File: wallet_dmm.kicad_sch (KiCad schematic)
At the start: 0 parts

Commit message: Added piezo driver oscillator (based on TLC555CDR) to schematic. Needs component values calculated for oscillator parameters (frequency, etc).
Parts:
- added C1, C2: 0.01uF, symbol Device:C_Small
- added C3: C, symbol Device:C_Small
- added R1, R2: R, symbol Device:R
- added U1: TLC555xD, Package_SO:SOIC-8_3.9x4.9mm_P1.27mm, symbol Timer:TLC555xD
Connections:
- new net: R1.2, R2.1, U1.7 (DIS)
- new net: C1.1, U1.5 (CV)
- new net: C3.1, R2.2, U1.2 (TR), U1.6 (THR)
- new net GND: C1.2, C2.2, C3.2, U1.1 (GND)
- new net OSC_OUT: U1.3 (Q)
- new net VCC: C2.1, R1.1, U1.4 (R), U1.8 (VCC)
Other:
- note added: "Piezo Driver Oscillator"

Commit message: saving work
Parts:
- added U2: STM32L051K8Tx, Package_QFP:LQFP-32_7x7mm_P0.8mm, symbol MCU_ST_STM32L0:STM32L051K8Tx
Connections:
- net GND: now also U2.16 (VSS), U2.32 (VSS)
- new net VDD: U2.1 (VDD), U2.17 (VDD)
- new net VDDA: U2.5 (VDDA)

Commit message: test2
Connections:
- net GND: no longer U2.16 (VSS), U2.32 (VSS)
- net VDD: no longer U2.1 (VDD), U2.17 (VDD)
- net VDDA: no longer U2.5 (VDDA)
- new net: U2.16 (VSS), U2.32 (VSS)
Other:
- moved on the sheet: U2
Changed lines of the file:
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@@
 	(symbol
 		(lib_id "MCU_ST_STM32L0:STM32L051K8Tx")
-		(at 58.42 102.87 0)
+		(at 49.53 102.87 0)
 		(unit 1)
 		(exclude_from_sim no)
@@
 		(fields_autoplaced yes)
 		(property "Reference" "U2"
-			(at 63.1541 128.27 0)
+			(at 54.2641 128.27 0)
 			(effects
 				(font
@@
 		)
 		(property "Value" "STM32L051K8Tx"
-			(at 63.1541 130.81 0)
+			(at 54.2641 130.81 0)
 			(effects
 				(font
@@
 		)
 		(property "Footprint" "Package_QFP:LQFP-32_7x7mm_P0.8mm"
-			(at 48.26 125.73 0)
+			(at 39.37 125.73 0)
 			(effects
 				(font
@@
 		)
 		(property "Datasheet" "https://www.st.com/resource/en/datasheet/stm32l051k8.pdf"
-			(at 58.42 102.87 0)
+			(at 49.53 102.87 0)
 			(effects
 				(font
@@
 		)
 		(property "Description" "STMicroelectronics Arm Cortex-M0+ MCU, 64KB flash, 8KB RAM, 32 MHz, 1.65-3.6V, 25 GPIO, LQFP32"
-			(at 58.42 102.87 0)
+			(at 49.53 102.87 0)
 			(effects
 				(font

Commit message: UPDATE SKETCH FILE
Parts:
- C3: value C -> 100nF
- R1: value R -> 1510R
- R2: value R -> 1000R
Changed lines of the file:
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@@
 			)
 		)
-		(property "Value" "R"
+		(property "Value" "1000R"
 			(at 74.93 41.9099 0)
 			(effects
@@
 			)
 		)
-		(property "Value" "R"
+		(property "Value" "1510R"
 			(at 74.93 29.2099 0)
 			(effects
@@
 			)
 		)
-		(property "Value" "C"
+		(property "Value" "100nF"
 			(at 74.93 52.0762 0)
 			(effects

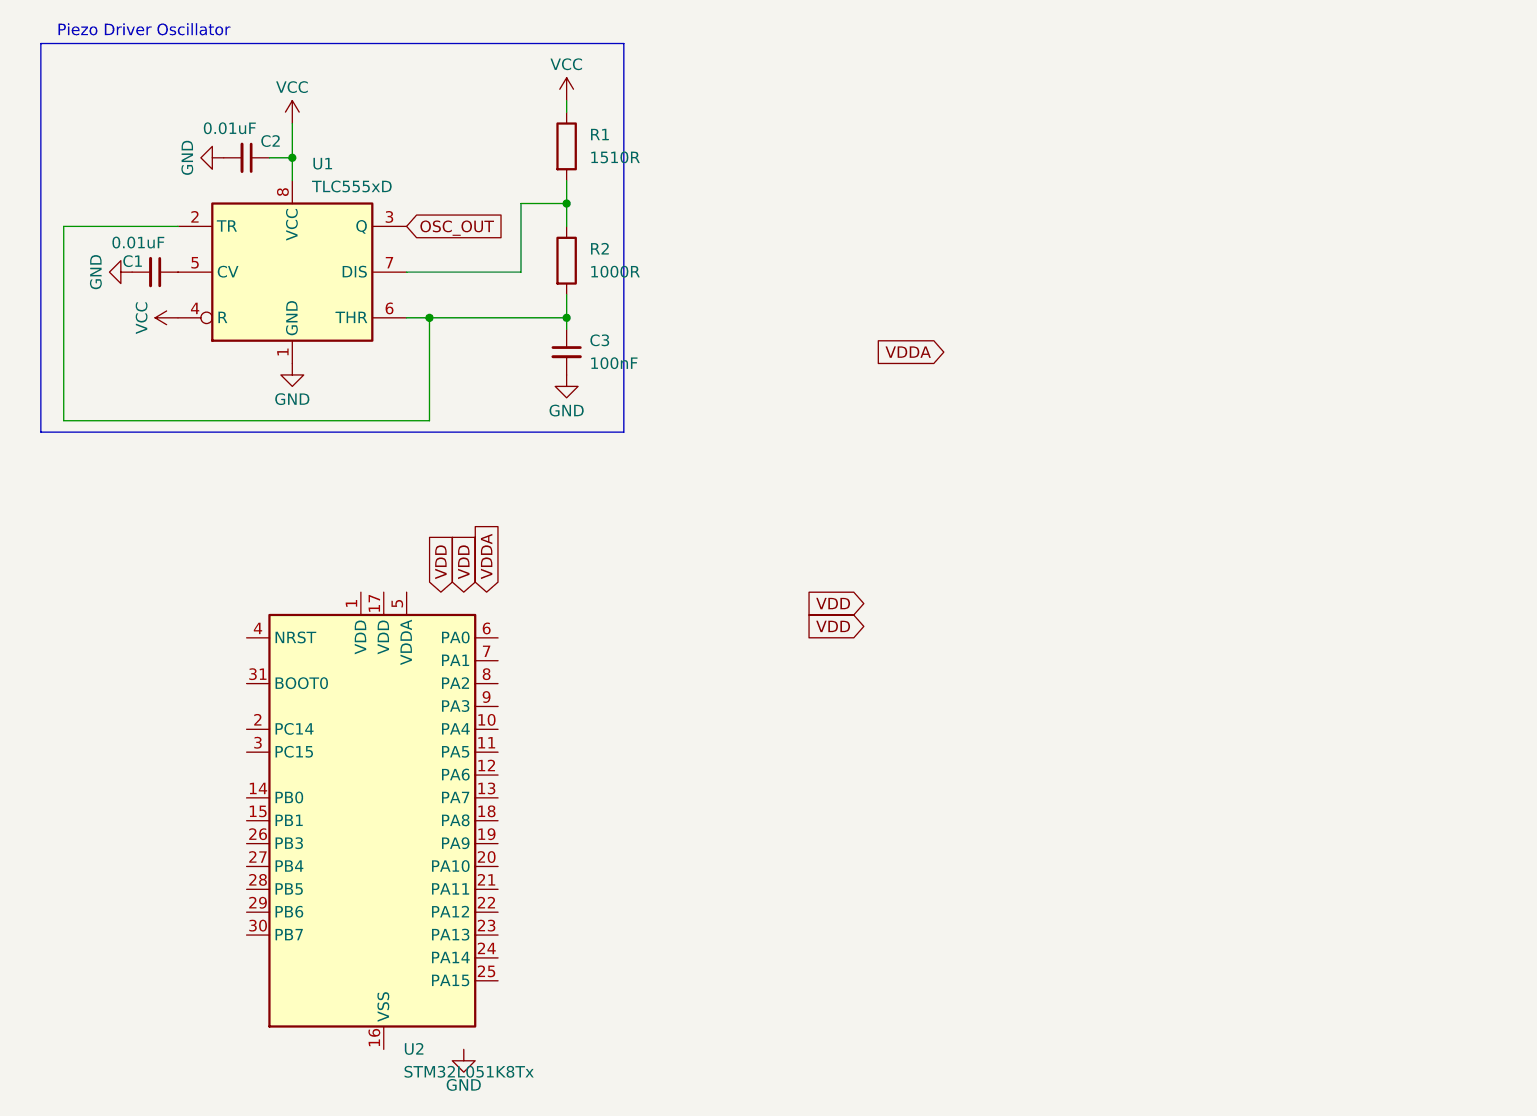
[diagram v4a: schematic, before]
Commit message: Added filter capacitors and reset button.
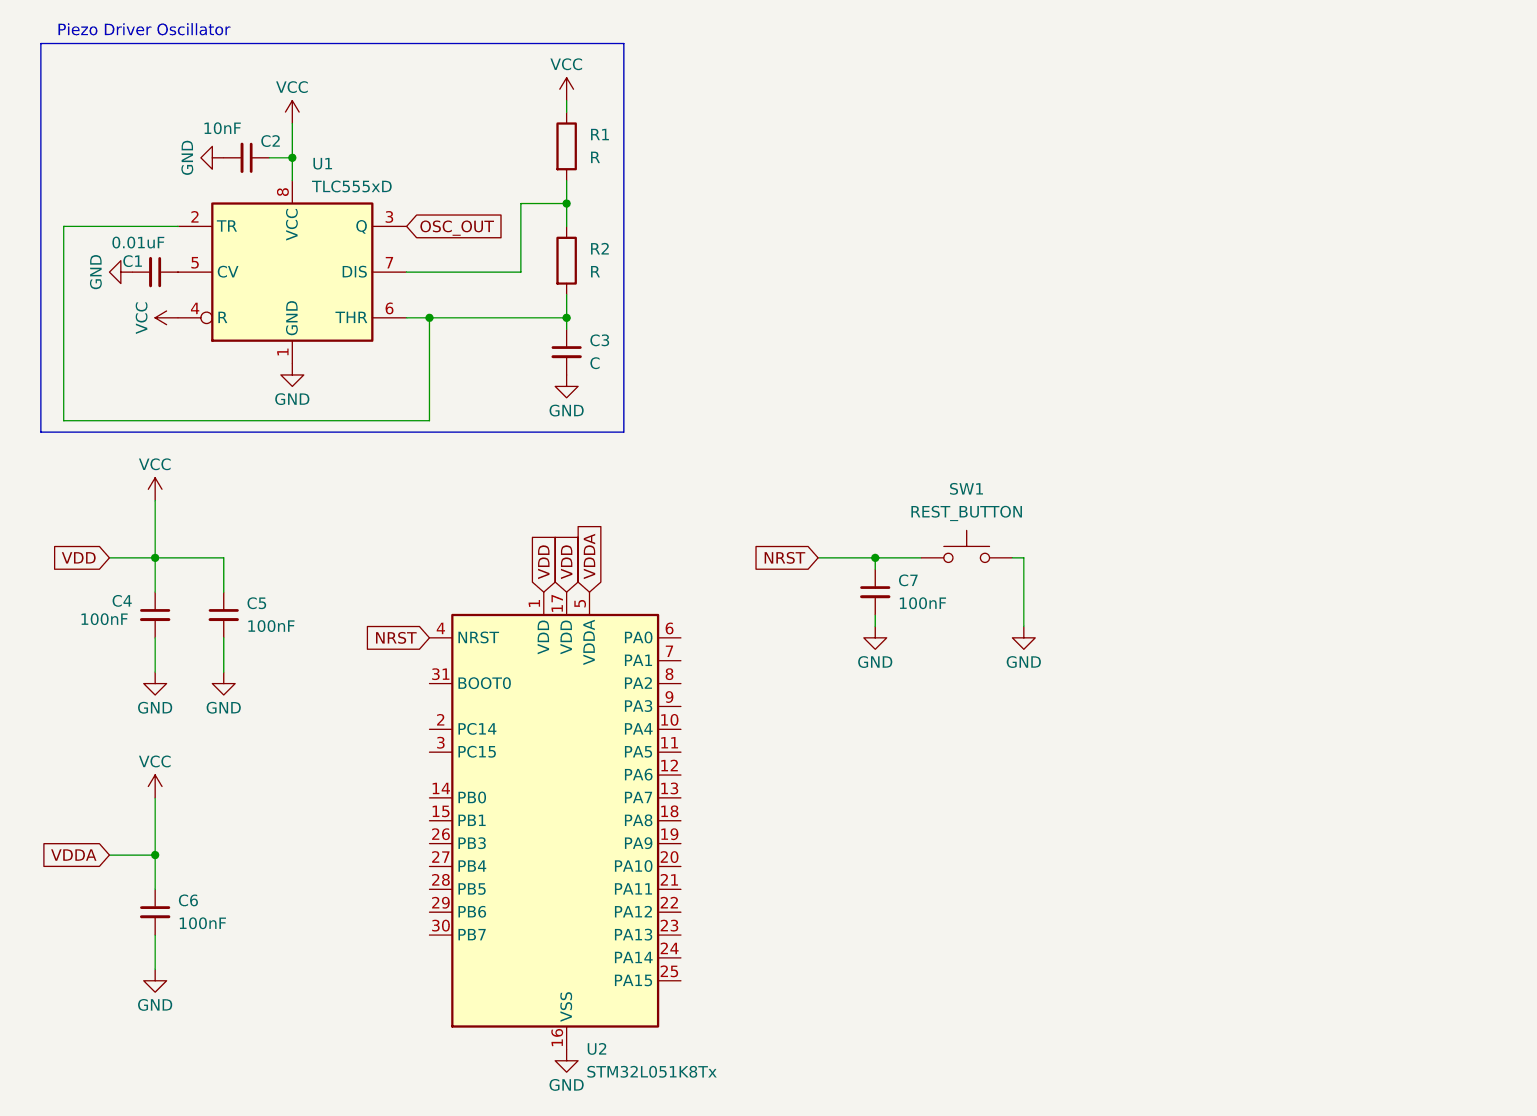
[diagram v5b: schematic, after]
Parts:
- added C4, C5, C6, C7: 100nF, symbol Device:C_Small
- added SW1: REST_BUTTON, symbol Switch:SW_MEC_5G
- C2: value 0.01uF -> 10nF
- C3: value 100nF -> C
- R1: value 1510R -> R
- R2: value 1000R -> R
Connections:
- net GND: now also U2.16 (VSS), U2.32 (VSS), C4.2, C5.2, C6.2, C7.2, SW1.3 (B), SW1.4 (B)
- net VCC: now also U2.1 (VDD), U2.17 (VDD), U2.5 (VDDA), C4.1, C5.1, C6.1
- net NRST: now reaches U2.4 (NRST)
- net NRST: now also C7.1, SW1.1 (A), SW1.2 (A)
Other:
- moved on the sheet: U2

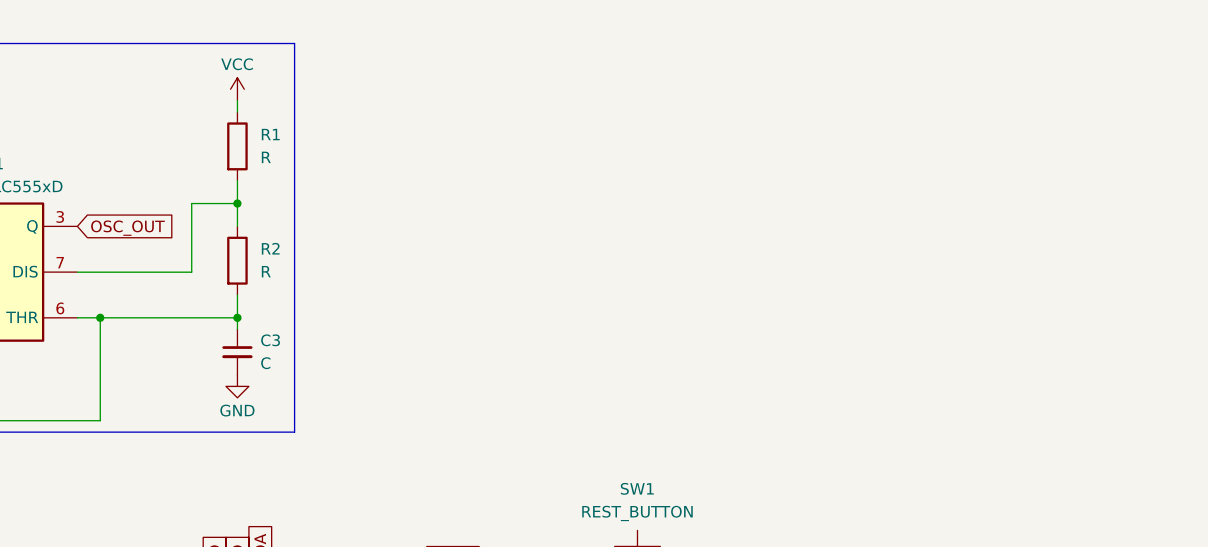
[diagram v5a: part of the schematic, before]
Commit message: Added back accidentally removed oscillator values.
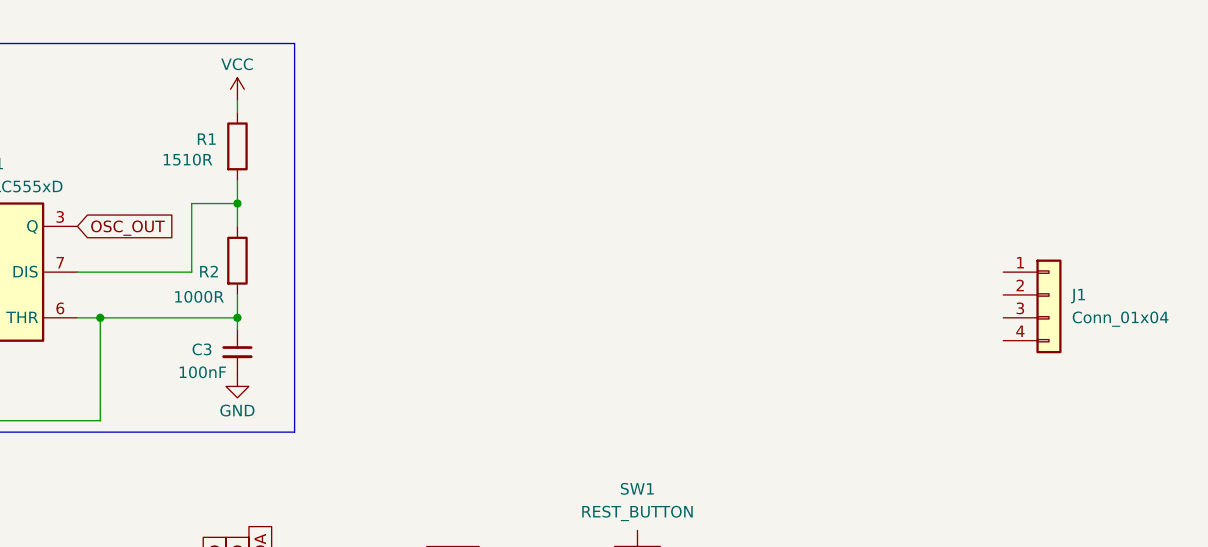
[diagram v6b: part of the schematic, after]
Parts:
- added J1: Conn_01x04, symbol Connector_Generic:Conn_01x04
- C3: value C -> 100nF
- R1: value R -> 1510R
- R2: value R -> 1000R
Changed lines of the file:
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@@
 		(on_board yes)
 		(dnp no)
-		(fields_autoplaced yes)
 		(property "Reference" "R2"
-			(at 74.93 39.3699 0)
-			(effects
-				(font
-					(size 1.27 1.27)
-				)
-				(justify left)
-			)
-		)
-		(property "Value" "R"
-			(at 74.93 41.9099 0)
+			(at 68.072 41.91 0)
+			(effects
+				(font
+					(size 1.27 1.27)
+				)
+				(justify left)
+			)
+		)
+		(property "Value" "1000R"
+			(at 65.278 44.704 0)
 			(effects
 				(font
@@
 	)
 	(symbol
+		(lib_id "Connector_Generic:Conn_01x04")
+		(at 162.56 44.45 0)
+		(unit 1)
+		(exclude_from_sim no)
+		(in_bom yes)
+		(on_board yes)
+		(dnp no)
+		(fields_autoplaced yes)
+		(property "Reference" "J1"
+			(at 165.1 44.4499 0)
+			(effects
+				(font
+					(size 1.27 1.27)
+				)
+				(justify left)
+			)
+		)
+		(property "Value" "Conn_01x04"
+			(at 165.1 46.9899 0)
+			(effects
+				(font
+					(size 1.27 1.27)
+				)
+				(justify left)
+			)
+		)
+		(property "Footprint" ""
+			(at 162.56 44.45 0)
+			(effects
+				(font
+					(size 1.27 1.27)
+				)
+				(hide yes)
+			)
+		)
+		(property "Datasheet" "~"
+			(at 162.56 44.45 0)
+			(effects
+				(font
+					(size 1.27 1.27)
+				)
+				(hide yes)
+			)
+		)
+		(property "Description" "Generic connector, single row, 01x04, script generated (kicad-library-utils/schlib/autogen/connector/)"
+			(at 162.56 44.45 0)
+			(effects
+				(font
+					(size 1.27 1.27)
+				)
+				(hide yes)
+			)
+		)
+		(pin "3"
+		)
+		(pin "2"
+		)
+		(pin "1"
+		)
+		(pin "4"
+		)
+		(instances
+			(project ""
+				(path "/2feb1339-af30-4942-92c0-e58400bfb20d"
+					(reference "J1")
+					(unit 1)
+				)
+			)
+		)
+	)
+	(symbol
 		(lib_id "Switch:SW_MEC_5G")
 		(at 116.84 73.66 0)
@@
 		(on_board yes)
 		(dnp no)
-		(fields_autoplaced yes)
 		(property "Reference" "R1"
-			(at 74.93 26.6699 0)
-			(effects
-				(font
-					(size 1.27 1.27)
-				)
-				(justify left)
-			)
-		)
-		(property "Value" "R"
-			(at 74.93 29.2099 0)
+			(at 67.818 27.178 0)
+			(effects
+				(font
+					(size 1.27 1.27)
+				)
+				(justify left)
+			)
+		)
+		(property "Value" "1510R"
+			(at 64.008 29.464 0)
 			(effects
 				(font
@@
 		(on_board yes)
 		(dnp no)
-		(fields_autoplaced yes)
 		(property "Reference" "C3"
-			(at 74.93 49.5362 0)
-			(effects
-				(font
-					(size 1.27 1.27)
-				)
-				(justify left)
-			)
-		)
-		(property "Value" "C"
-			(at 74.93 52.0762 0)
-			(effects
-				(font
+			(at 67.31 50.546 0)
+			(effects
+				(font
+					(size 1.27 1.27)
+				)
+				(justify left)
+			)
+		)
+		(property "Value" "100nF"
+			(at 65.786 53.086 0)
+			(effects
+				(font
